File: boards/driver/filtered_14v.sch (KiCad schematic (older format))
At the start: 2 parts

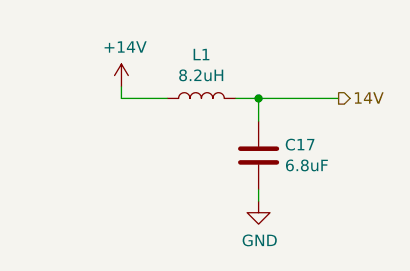
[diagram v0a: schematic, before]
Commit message: Driver board: finished first rough draft schematic. Lots of placeholders, but at least every place is held.
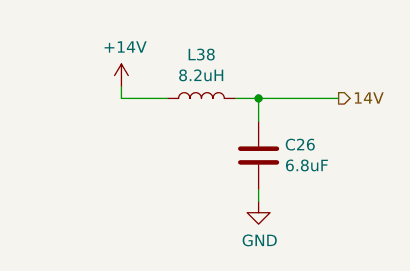
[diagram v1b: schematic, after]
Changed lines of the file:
@@
 $Descr A4 11693 8268
 encoding utf-8
-Sheet 3 68
+Sheet 3 69
 Title ""
 Date ""
@@
 AR Path="/6183FAE6/61E0F0ED/625192D8" Ref="L?"  Part="1"
 AR Path="/61EC7443/61E13129/625192D8" Ref="L1"  Part="1"
-F 0 "L1" V 5490 3800 50  0000 C CNN
+F 0 "L38" V 5490 3800 50  0000 C CNN
 F 1 "8.2uH" V 5399 3800 50  0000 C CNN
 F 2 "" H 5300 3800 50  0001 C CNN
@@
 AR Path="/6183FAE6/61E0F0ED/6251BD30" Ref="C?"  Part="1"
 AR Path="/61EC7443/61E13129/6251BD30" Ref="C17"  Part="1"
-F 0 "C17" H 5665 4096 50  0000 L CNN
+F 0 "C26" H 5665 4096 50  0000 L CNN
 F 1 "6.8uF" H 5665 4005 50  0000 L CNN
 F 2 "" H 5588 3900 50  0001 C CNN

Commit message: Driver board: fleshed out the hotswap controller, tweaked some resistors, and added some bypass caps
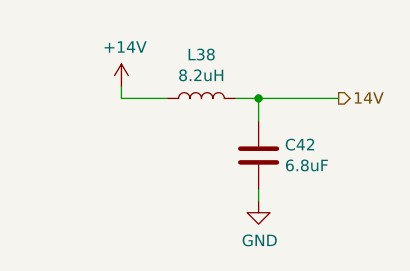
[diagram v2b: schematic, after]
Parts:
- renumbered C19 to C35
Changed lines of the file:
@@
 $EndComp
 $Comp
-L lachesis:+14V #PWR086
+L lachesis:+14V #PWR089
 U 1 1 62519A3E
 P 4950 3750
-AR Path="/6183FAE6/62519032/62519A3E" Ref="#PWR086"  Part="1"
-AR Path="/6183FAE6/62531DCA/62519A3E" Ref="#PWR088"  Part="1"
-AR Path="/6183FAE6/6254620B/62519A3E" Ref="#PWR090"  Part="1"
+AR Path="/6183FAE6/62519032/62519A3E" Ref="#PWR089"  Part="1"
+AR Path="/6183FAE6/62531DCA/62519A3E" Ref="#PWR091"  Part="1"
+AR Path="/6183FAE6/6254620B/62519A3E" Ref="#PWR093"  Part="1"
 AR Path="/6183FAE6/62546210/62519A3E" Ref="#PWR?"  Part="1"
-AR Path="/6183FAE6/62630A14/62519A3E" Ref="#PWR092"  Part="1"
-AR Path="/6183FAE6/62637D4C/62519A3E" Ref="#PWR094"  Part="1"
-AR Path="/6183FAE6/626621B6/62519A3E" Ref="#PWR096"  Part="1"
-AR Path="/6183FAE6/626621BA/62519A3E" Ref="#PWR098"  Part="1"
-AR Path="/6183FAE6/626621BF/62519A3E" Ref="#PWR0100"  Part="1"
-AR Path="/64D2DF1E/62A035A1/62519A3E" Ref="#PWR035"  Part="1"
+AR Path="/6183FAE6/62630A14/62519A3E" Ref="#PWR095"  Part="1"
+AR Path="/6183FAE6/62637D4C/62519A3E" Ref="#PWR097"  Part="1"
+AR Path="/6183FAE6/626621B6/62519A3E" Ref="#PWR099"  Part="1"
+AR Path="/6183FAE6/626621BA/62519A3E" Ref="#PWR0101"  Part="1"
+AR Path="/6183FAE6/626621BF/62519A3E" Ref="#PWR0103"  Part="1"
+AR Path="/64D2DF1E/62A035A1/62519A3E" Ref="#PWR038"  Part="1"
 AR Path="/6183FAE6/61E0F0ED/62519A3E" Ref="#PWR?"  Part="1"
-AR Path="/61EC7443/61E13129/62519A3E" Ref="#PWR033"  Part="1"
-F 0 "#PWR0100" H 4950 3600 50  0001 C CNN
+AR Path="/61EC7443/61E13129/62519A3E" Ref="#PWR036"  Part="1"
+F 0 "#PWR0103" H 4950 3600 50  0001 C CNN
 F 1 "+14V" H 4965 3923 50  0000 C CNN
 F 2 "" H 4950 3750 50  0001 C CNN
@@
 	5550 3800 5550 3900
 $Comp
-L Device:C C19
+L Device:C C35
 U 1 1 6251BD30
 P 5550 4050
-AR Path="/6183FAE6/62519032/6251BD30" Ref="C19"  Part="1"
-AR Path="/6183FAE6/62531DCA/6251BD30" Ref="C20"  Part="1"
-AR Path="/6183FAE6/6254620B/6251BD30" Ref="C21"  Part="1"
+AR Path="/6183FAE6/62519032/6251BD30" Ref="C35"  Part="1"
+AR Path="/6183FAE6/62531DCA/6251BD30" Ref="C36"  Part="1"
+AR Path="/6183FAE6/6254620B/6251BD30" Ref="C37"  Part="1"
 AR Path="/6183FAE6/62546210/6251BD30" Ref="C?"  Part="1"
-AR Path="/6183FAE6/62630A14/6251BD30" Ref="C22"  Part="1"
-AR Path="/6183FAE6/62637D4C/6251BD30" Ref="C23"  Part="1"
-AR Path="/6183FAE6/626621B6/6251BD30" Ref="C24"  Part="1"
-AR Path="/6183FAE6/626621BA/6251BD30" Ref="C25"  Part="1"
-AR Path="/6183FAE6/626621BF/6251BD30" Ref="C26"  Part="1"
-AR Path="/64D2DF1E/62A035A1/6251BD30" Ref="C18"  Part="1"
+AR Path="/6183FAE6/62630A14/6251BD30" Ref="C38"  Part="1"
+AR Path="/6183FAE6/62637D4C/6251BD30" Ref="C39"  Part="1"
+AR Path="/6183FAE6/626621B6/6251BD30" Ref="C40"  Part="1"
+AR Path="/6183FAE6/626621BA/6251BD30" Ref="C41"  Part="1"
+AR Path="/6183FAE6/626621BF/6251BD30" Ref="C42"  Part="1"
+AR Path="/64D2DF1E/62A035A1/6251BD30" Ref="C34"  Part="1"
 AR Path="/6183FAE6/61E0F0ED/6251BD30" Ref="C?"  Part="1"
-AR Path="/61EC7443/61E13129/6251BD30" Ref="C17"  Part="1"
-F 0 "C26" H 5665 4096 50  0000 L CNN
+AR Path="/61EC7443/61E13129/6251BD30" Ref="C33"  Part="1"
+F 0 "C42" H 5665 4096 50  0000 L CNN
 F 1 "6.8uF" H 5665 4005 50  0000 L CNN
 F 2 "" H 5588 3900 50  0001 C CNN
@@
 	5550 4200 5550 4250
 $Comp
-L power:GND #PWR087
+L power:GND #PWR090
 U 1 1 6251C31D
 P 5550 4250
-AR Path="/6183FAE6/62519032/6251C31D" Ref="#PWR087"  Part="1"
-AR Path="/6183FAE6/62531DCA/6251C31D" Ref="#PWR089"  Part="1"
-AR Path="/6183FAE6/6254620B/6251C31D" Ref="#PWR091"  Part="1"
+AR Path="/6183FAE6/62519032/6251C31D" Ref="#PWR090"  Part="1"
+AR Path="/6183FAE6/62531DCA/6251C31D" Ref="#PWR092"  Part="1"
+AR Path="/6183FAE6/6254620B/6251C31D" Ref="#PWR094"  Part="1"
 AR Path="/6183FAE6/62546210/6251C31D" Ref="#PWR?"  Part="1"
-AR Path="/6183FAE6/62630A14/6251C31D" Ref="#PWR093"  Part="1"
-AR Path="/6183FAE6/62637D4C/6251C31D" Ref="#PWR095"  Part="1"
-AR Path="/6183FAE6/626621B6/6251C31D" Ref="#PWR097"  Part="1"
-AR Path="/6183FAE6/626621BA/6251C31D" Ref="#PWR099"  Part="1"
-AR Path="/6183FAE6/626621BF/6251C31D" Ref="#PWR0101"  Part="1"
-AR Path="/64D2DF1E/62A035A1/6251C31D" Ref="#PWR036"  Part="1"
+AR Path="/6183FAE6/62630A14/6251C31D" Ref="#PWR096"  Part="1"
+AR Path="/6183FAE6/62637D4C/6251C31D" Ref="#PWR098"  Part="1"
+AR Path="/6183FAE6/626621B6/6251C31D" Ref="#PWR0100"  Part="1"
+AR Path="/6183FAE6/626621BA/6251C31D" Ref="#PWR0102"  Part="1"
+AR Path="/6183FAE6/626621BF/6251C31D" Ref="#PWR0104"  Part="1"
+AR Path="/64D2DF1E/62A035A1/6251C31D" Ref="#PWR039"  Part="1"
 AR Path="/6183FAE6/61E0F0ED/6251C31D" Ref="#PWR?"  Part="1"
-AR Path="/61EC7443/61E13129/6251C31D" Ref="#PWR034"  Part="1"
-F 0 "#PWR0101" H 5550 4000 50  0001 C CNN
+AR Path="/61EC7443/61E13129/6251C31D" Ref="#PWR037"  Part="1"
+F 0 "#PWR0104" H 5550 4000 50  0001 C CNN
 F 1 "GND" H 5555 4077 50  0000 C CNN
 F 2 "" H 5550 4250 50  0001 C CNN

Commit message: Driver board: significant cleanup. Moved sense amp pairs into a subsheet, split tuning resistors into two globally, pushed input circuits into their corresponding sheets.
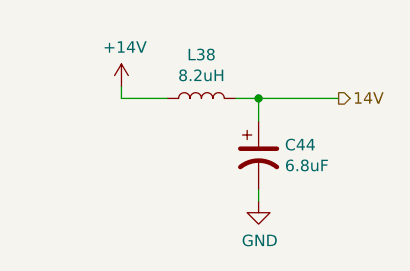
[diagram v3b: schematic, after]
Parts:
- removed C35: 6.8uF, symbol Device:C
- added C3: 6.8uF, Capacitor_Tantalum_SMD:CP_EIA-7343-31_Kemet-D, symbol Device:CP1
- L31: footprint (none) -> Inductor_SMD:L_1812_4532Metric
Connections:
- net 14V: now also C3.1
- net GND: now also C3.2
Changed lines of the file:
@@
 $Descr A4 11693 8268
 encoding utf-8
-Sheet 3 69
+Sheet 56 64
 Title ""
 Date ""
@@
 F 0 "L38" V 5490 3800 50  0000 C CNN
 F 1 "8.2uH" V 5399 3800 50  0000 C CNN
-F 2 "" H 5300 3800 50  0001 C CNN
+F 2 "Inductor_SMD:L_1812_4532Metric" H 5300 3800 50  0001 C CNN
 F 3 "~" H 5300 3800 50  0001 C CNN
 	1    5300 3800
@@
 $EndComp
 $Comp
-L lachesis:+14V #PWR089
+L lachesis:+14V #PWR0106
 U 1 1 62519A3E
 P 4950 3750
-AR Path="/6183FAE6/62519032/62519A3E" Ref="#PWR089"  Part="1"
-AR Path="/6183FAE6/62531DCA/62519A3E" Ref="#PWR091"  Part="1"
-AR Path="/6183FAE6/6254620B/62519A3E" Ref="#PWR093"  Part="1"
+AR Path="/6183FAE6/62519032/62519A3E" Ref="#PWR0106"  Part="1"
+AR Path="/6183FAE6/62531DCA/62519A3E" Ref="#PWR0108"  Part="1"
+AR Path="/6183FAE6/6254620B/62519A3E" Ref="#PWR0110"  Part="1"
 AR Path="/6183FAE6/62546210/62519A3E" Ref="#PWR?"  Part="1"
-AR Path="/6183FAE6/62630A14/62519A3E" Ref="#PWR095"  Part="1"
-AR Path="/6183FAE6/62637D4C/62519A3E" Ref="#PWR097"  Part="1"
-AR Path="/6183FAE6/626621B6/62519A3E" Ref="#PWR099"  Part="1"
-AR Path="/6183FAE6/626621BA/62519A3E" Ref="#PWR0101"  Part="1"
-AR Path="/6183FAE6/626621BF/62519A3E" Ref="#PWR0103"  Part="1"
-AR Path="/64D2DF1E/62A035A1/62519A3E" Ref="#PWR038"  Part="1"
+AR Path="/6183FAE6/62630A14/62519A3E" Ref="#PWR0112"  Part="1"
+AR Path="/6183FAE6/62637D4C/62519A3E" Ref="#PWR0114"  Part="1"
+AR Path="/6183FAE6/626621B6/62519A3E" Ref="#PWR0116"  Part="1"
+AR Path="/6183FAE6/626621BA/62519A3E" Ref="#PWR0118"  Part="1"
+AR Path="/6183FAE6/626621BF/62519A3E" Ref="#PWR0120"  Part="1"
+AR Path="/64D2DF1E/62A035A1/62519A3E" Ref="#PWR056"  Part="1"
 AR Path="/6183FAE6/61E0F0ED/62519A3E" Ref="#PWR?"  Part="1"
-AR Path="/61EC7443/61E13129/62519A3E" Ref="#PWR036"  Part="1"
-F 0 "#PWR0103" H 4950 3600 50  0001 C CNN
+AR Path="/61EC7443/61E13129/62519A3E" Ref="#PWR05"  Part="1"
+F 0 "#PWR0120" H 4950 3600 50  0001 C CNN
 F 1 "+14V" H 4965 3923 50  0000 C CNN
 F 2 "" H 4950 3750 50  0001 C CNN
@@
 Wire Wire Line
 	5550 3800 5550 3900
-$Comp
-L Device:C C35
-U 1 1 6251BD30
-P 5550 4050
-AR Path="/6183FAE6/62519032/6251BD30" Ref="C35"  Part="1"
-AR Path="/6183FAE6/62531DCA/6251BD30" Ref="C36"  Part="1"
-AR Path="/6183FAE6/6254620B/6251BD30" Ref="C37"  Part="1"
-AR Path="/6183FAE6/62546210/6251BD30" Ref="C?"  Part="1"
-AR Path="/6183FAE6/62630A14/6251BD30" Ref="C38"  Part="1"
-AR Path="/6183FAE6/62637D4C/6251BD30" Ref="C39"  Part="1"
-AR Path="/6183FAE6/626621B6/6251BD30" Ref="C40"  Part="1"
-AR Path="/6183FAE6/626621BA/6251BD30" Ref="C41"  Part="1"
-AR Path="/6183FAE6/626621BF/6251BD30" Ref="C42"  Part="1"
-AR Path="/64D2DF1E/62A035A1/6251BD30" Ref="C34"  Part="1"
-AR Path="/6183FAE6/61E0F0ED/6251BD30" Ref="C?"  Part="1"
-AR Path="/61EC7443/61E13129/6251BD30" Ref="C33"  Part="1"
-F 0 "C42" H 5665 4096 50  0000 L CNN
-F 1 "6.8uF" H 5665 4005 50  0000 L CNN
-F 2 "" H 5588 3900 50  0001 C CNN
-F 3 "~" H 5550 4050 50  0001 C CNN
-	1    5550 4050
-	1    0    0    -1
-$EndComp
 Wire Wire Line
 	5550 4200 5550 4250
 $Comp
-L power:GND #PWR090
+L power:GND #PWR0107
 U 1 1 6251C31D
 P 5550 4250
-AR Path="/6183FAE6/62519032/6251C31D" Ref="#PWR090"  Part="1"
-AR Path="/6183FAE6/62531DCA/6251C31D" Ref="#PWR092"  Part="1"
-AR Path="/6183FAE6/6254620B/6251C31D" Ref="#PWR094"  Part="1"
+AR Path="/6183FAE6/62519032/6251C31D" Ref="#PWR0107"  Part="1"
+AR Path="/6183FAE6/62531DCA/6251C31D" Ref="#PWR0109"  Part="1"
+AR Path="/6183FAE6/6254620B/6251C31D" Ref="#PWR0111"  Part="1"
 AR Path="/6183FAE6/62546210/6251C31D" Ref="#PWR?"  Part="1"
-AR Path="/6183FAE6/62630A14/6251C31D" Ref="#PWR096"  Part="1"
-AR Path="/6183FAE6/62637D4C/6251C31D" Ref="#PWR098"  Part="1"
-AR Path="/6183FAE6/626621B6/6251C31D" Ref="#PWR0100"  Part="1"
-AR Path="/6183FAE6/626621BA/6251C31D" Ref="#PWR0102"  Part="1"
-AR Path="/6183FAE6/626621BF/6251C31D" Ref="#PWR0104"  Part="1"
-AR Path="/64D2DF1E/62A035A1/6251C31D" Ref="#PWR039"  Part="1"
+AR Path="/6183FAE6/62630A14/6251C31D" Ref="#PWR0113"  Part="1"
+AR Path="/6183FAE6/62637D4C/6251C31D" Ref="#PWR0115"  Part="1"
+AR Path="/6183FAE6/626621B6/6251C31D" Ref="#PWR0117"  Part="1"
+AR Path="/6183FAE6/626621BA/6251C31D" Ref="#PWR0119"  Part="1"
+AR Path="/6183FAE6/626621BF/6251C31D" Ref="#PWR0121"  Part="1"
+AR Path="/64D2DF1E/62A035A1/6251C31D" Ref="#PWR057"  Part="1"
 AR Path="/6183FAE6/61E0F0ED/6251C31D" Ref="#PWR?"  Part="1"
-AR Path="/61EC7443/61E13129/6251C31D" Ref="#PWR037"  Part="1"
-F 0 "#PWR0104" H 5550 4000 50  0001 C CNN
+AR Path="/61EC7443/61E13129/6251C31D" Ref="#PWR06"  Part="1"
+F 0 "#PWR0121" H 5550 4000 50  0001 C CNN
 F 1 "GND" H 5555 4077 50  0000 C CNN
 F 2 "" H 5550 4250 50  0001 C CNN
@@
 Text HLabel 5900 3800 2    50   Output ~ 0
 14V
+$Comp
+L Device:CP1 C3
+U 1 1 628400BF
+P 5550 4050
+AR Path="/61EC7443/61E13129/628400BF" Ref="C3"  Part="1"
+AR Path="/6183FAE6/62637D4C/628400BF" Ref="C41"  Part="1"
+AR Path="/64D2DF1E/62A035A1/628400BF" Ref="C36"  Part="1"
+AR Path="/6183FAE6/62519032/628400BF" Ref="C37"  Part="1"
+AR Path="/6183FAE6/62531DCA/628400BF" Ref="C38"  Part="1"
+AR Path="/6183FAE6/6254620B/628400BF" Ref="C39"  Part="1"
+AR Path="/6183FAE6/62630A14/628400BF" Ref="C40"  Part="1"
+AR Path="/6183FAE6/626621B6/628400BF" Ref="C42"  Part="1"
+AR Path="/6183FAE6/626621BA/628400BF" Ref="C43"  Part="1"
+AR Path="/6183FAE6/626621BF/628400BF" Ref="C44"  Part="1"
+F 0 "C44" H 5665 4096 50  0000 L CNN
+F 1 "6.8uF" H 5665 4005 50  0000 L CNN
+F 2 "Capacitor_Tantalum_SMD:CP_EIA-7343-31_Kemet-D" H 5550 4050 50  0001 C CNN
+F 3 "~" H 5550 4050 50  0001 C CNN
+	1    5550 4050
+	1    0    0    -1
+$EndComp
 $EndSCHEMATC

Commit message: Driver board: integrated DIN 41612 backplane connector, and made a dedicated parity inhibit sheet with a different set resistor value.
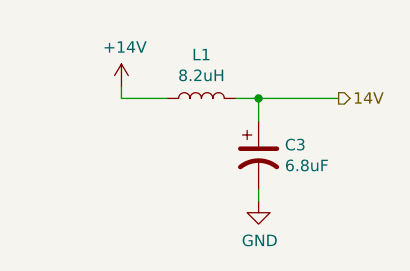
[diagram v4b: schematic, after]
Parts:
- renumbered L31 to L29
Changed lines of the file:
@@
 $Descr A4 11693 8268
 encoding utf-8
-Sheet 56 64
+Sheet 3 64
 Title ""
 Date ""
@@
 $EndDescr
 $Comp
-L Device:L L31
+L Device:L L29
 U 1 1 625192D8
 P 5300 3800
-AR Path="/6183FAE6/62519032/625192D8" Ref="L31"  Part="1"
-AR Path="/6183FAE6/62531DCA/625192D8" Ref="L32"  Part="1"
-AR Path="/6183FAE6/6254620B/625192D8" Ref="L33"  Part="1"
+AR Path="/6183FAE6/62519032/625192D8" Ref="L29"  Part="1"
+AR Path="/6183FAE6/62531DCA/625192D8" Ref="L30"  Part="1"
+AR Path="/6183FAE6/6254620B/625192D8" Ref="L31"  Part="1"
 AR Path="/6183FAE6/62546210/625192D8" Ref="L?"  Part="1"
-AR Path="/6183FAE6/62630A14/625192D8" Ref="L34"  Part="1"
-AR Path="/6183FAE6/62637D4C/625192D8" Ref="L35"  Part="1"
-AR Path="/6183FAE6/626621B6/625192D8" Ref="L36"  Part="1"
-AR Path="/6183FAE6/626621BA/625192D8" Ref="L37"  Part="1"
-AR Path="/6183FAE6/626621BF/625192D8" Ref="L38"  Part="1"
+AR Path="/6183FAE6/62630A14/625192D8" Ref="L32"  Part="1"
+AR Path="/6183FAE6/62637D4C/625192D8" Ref="L33"  Part="1"
+AR Path="/6183FAE6/626621B6/625192D8" Ref="L34"  Part="1"
+AR Path="/6183FAE6/626621BA/625192D8" Ref="L35"  Part="1"
+AR Path="/6183FAE6/626621BF/625192D8" Ref="L36"  Part="1"
 AR Path="/64D2DF1E/62A035A1/625192D8" Ref="L2"  Part="1"
 AR Path="/6183FAE6/61E0F0ED/625192D8" Ref="L?"  Part="1"
 AR Path="/61EC7443/61E13129/625192D8" Ref="L1"  Part="1"
-F 0 "L38" V 5490 3800 50  0000 C CNN
+F 0 "L1" V 5490 3800 50  0000 C CNN
 F 1 "8.2uH" V 5399 3800 50  0000 C CNN
 F 2 "Inductor_SMD:L_1812_4532Metric" H 5300 3800 50  0001 C CNN
@@
 $EndComp
 $Comp
-L lachesis:+14V #PWR0106
+L lachesis:+14V #PWR0105
 U 1 1 62519A3E
 P 4950 3750
-AR Path="/6183FAE6/62519032/62519A3E" Ref="#PWR0106"  Part="1"
-AR Path="/6183FAE6/62531DCA/62519A3E" Ref="#PWR0108"  Part="1"
-AR Path="/6183FAE6/6254620B/62519A3E" Ref="#PWR0110"  Part="1"
+AR Path="/6183FAE6/62519032/62519A3E" Ref="#PWR0105"  Part="1"
+AR Path="/6183FAE6/62531DCA/62519A3E" Ref="#PWR0107"  Part="1"
+AR Path="/6183FAE6/6254620B/62519A3E" Ref="#PWR0109"  Part="1"
 AR Path="/6183FAE6/62546210/62519A3E" Ref="#PWR?"  Part="1"
-AR Path="/6183FAE6/62630A14/62519A3E" Ref="#PWR0112"  Part="1"
-AR Path="/6183FAE6/62637D4C/62519A3E" Ref="#PWR0114"  Part="1"
-AR Path="/6183FAE6/626621B6/62519A3E" Ref="#PWR0116"  Part="1"
-AR Path="/6183FAE6/626621BA/62519A3E" Ref="#PWR0118"  Part="1"
-AR Path="/6183FAE6/626621BF/62519A3E" Ref="#PWR0120"  Part="1"
-AR Path="/64D2DF1E/62A035A1/62519A3E" Ref="#PWR056"  Part="1"
+AR Path="/6183FAE6/62630A14/62519A3E" Ref="#PWR0111"  Part="1"
+AR Path="/6183FAE6/62637D4C/62519A3E" Ref="#PWR0113"  Part="1"
+AR Path="/6183FAE6/626621B6/62519A3E" Ref="#PWR0115"  Part="1"
+AR Path="/6183FAE6/626621BA/62519A3E" Ref="#PWR0117"  Part="1"
+AR Path="/6183FAE6/626621BF/62519A3E" Ref="#PWR0119"  Part="1"
+AR Path="/64D2DF1E/62A035A1/62519A3E" Ref="#PWR057"  Part="1"
 AR Path="/6183FAE6/61E0F0ED/62519A3E" Ref="#PWR?"  Part="1"
 AR Path="/61EC7443/61E13129/62519A3E" Ref="#PWR05"  Part="1"
-F 0 "#PWR0120" H 4950 3600 50  0001 C CNN
+F 0 "#PWR05" H 4950 3600 50  0001 C CNN
 F 1 "+14V" H 4965 3923 50  0000 C CNN
 F 2 "" H 4950 3750 50  0001 C CNN
@@
 	5550 4200 5550 4250
 $Comp
-L power:GND #PWR0107
+L power:GND #PWR0106
 U 1 1 6251C31D
 P 5550 4250
-AR Path="/6183FAE6/62519032/6251C31D" Ref="#PWR0107"  Part="1"
-AR Path="/6183FAE6/62531DCA/6251C31D" Ref="#PWR0109"  Part="1"
-AR Path="/6183FAE6/6254620B/6251C31D" Ref="#PWR0111"  Part="1"
+AR Path="/6183FAE6/62519032/6251C31D" Ref="#PWR0106"  Part="1"
+AR Path="/6183FAE6/62531DCA/6251C31D" Ref="#PWR0108"  Part="1"
+AR Path="/6183FAE6/6254620B/6251C31D" Ref="#PWR0110"  Part="1"
 AR Path="/6183FAE6/62546210/6251C31D" Ref="#PWR?"  Part="1"
-AR Path="/6183FAE6/62630A14/6251C31D" Ref="#PWR0113"  Part="1"
-AR Path="/6183FAE6/62637D4C/6251C31D" Ref="#PWR0115"  Part="1"
-AR Path="/6183FAE6/626621B6/6251C31D" Ref="#PWR0117"  Part="1"
-AR Path="/6183FAE6/626621BA/6251C31D" Ref="#PWR0119"  Part="1"
-AR Path="/6183FAE6/626621BF/6251C31D" Ref="#PWR0121"  Part="1"
-AR Path="/64D2DF1E/62A035A1/6251C31D" Ref="#PWR057"  Part="1"
+AR Path="/6183FAE6/62630A14/6251C31D" Ref="#PWR0112"  Part="1"
+AR Path="/6183FAE6/62637D4C/6251C31D" Ref="#PWR0114"  Part="1"
+AR Path="/6183FAE6/626621B6/6251C31D" Ref="#PWR0116"  Part="1"
+AR Path="/6183FAE6/626621BA/6251C31D" Ref="#PWR0118"  Part="1"
+AR Path="/6183FAE6/626621BF/6251C31D" Ref="#PWR0120"  Part="1"
+AR Path="/64D2DF1E/62A035A1/6251C31D" Ref="#PWR058"  Part="1"
 AR Path="/6183FAE6/61E0F0ED/6251C31D" Ref="#PWR?"  Part="1"
 AR Path="/61EC7443/61E13129/6251C31D" Ref="#PWR06"  Part="1"
-F 0 "#PWR0121" H 5550 4000 50  0001 C CNN
+F 0 "#PWR06" H 5550 4000 50  0001 C CNN
 F 1 "GND" H 5555 4077 50  0000 C CNN
 F 2 "" H 5550 4250 50  0001 C CNN
@@
 AR Path="/6183FAE6/626621BA/628400BF" Ref="C43"  Part="1"
 AR Path="/6183FAE6/626621BF/628400BF" Ref="C44"  Part="1"
-F 0 "C44" H 5665 4096 50  0000 L CNN
+F 0 "C3" H 5665 4096 50  0000 L CNN
 F 1 "6.8uF" H 5665 4005 50  0000 L CNN
 F 2 "Capacitor_Tantalum_SMD:CP_EIA-7343-31_Kemet-D" H 5550 4050 50  0001 C CNN

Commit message: Driver: incorporated some power LEDs
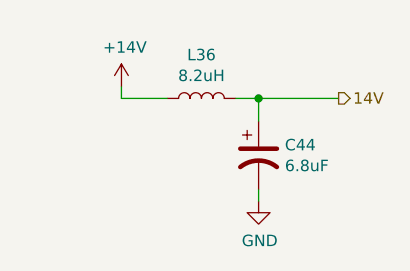
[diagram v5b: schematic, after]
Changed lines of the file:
@@
 AR Path="/6183FAE6/61E0F0ED/625192D8" Ref="L?"  Part="1"
 AR Path="/61EC7443/61E13129/625192D8" Ref="L1"  Part="1"
-F 0 "L1" V 5490 3800 50  0000 C CNN
+F 0 "L36" V 5490 3800 50  0000 C CNN
 F 1 "8.2uH" V 5399 3800 50  0000 C CNN
 F 2 "Inductor_SMD:L_1812_4532Metric" H 5300 3800 50  0001 C CNN
@@
 AR Path="/6183FAE6/61E0F0ED/62519A3E" Ref="#PWR?"  Part="1"
 AR Path="/61EC7443/61E13129/62519A3E" Ref="#PWR05"  Part="1"
-F 0 "#PWR05" H 4950 3600 50  0001 C CNN
+F 0 "#PWR0119" H 4950 3600 50  0001 C CNN
 F 1 "+14V" H 4965 3923 50  0000 C CNN
 F 2 "" H 4950 3750 50  0001 C CNN
@@
 AR Path="/6183FAE6/61E0F0ED/6251C31D" Ref="#PWR?"  Part="1"
 AR Path="/61EC7443/61E13129/6251C31D" Ref="#PWR06"  Part="1"
-F 0 "#PWR06" H 5550 4000 50  0001 C CNN
+F 0 "#PWR0120" H 5550 4000 50  0001 C CNN
 F 1 "GND" H 5555 4077 50  0000 C CNN
 F 2 "" H 5550 4250 50  0001 C CNN
@@
 AR Path="/6183FAE6/626621BA/628400BF" Ref="C43"  Part="1"
 AR Path="/6183FAE6/626621BF/628400BF" Ref="C44"  Part="1"
-F 0 "C3" H 5665 4096 50  0000 L CNN
+F 0 "C44" H 5665 4096 50  0000 L CNN
 F 1 "6.8uF" H 5665 4005 50  0000 L CNN
 F 2 "Capacitor_Tantalum_SMD:CP_EIA-7343-31_Kemet-D" H 5550 4050 50  0001 C CNN
